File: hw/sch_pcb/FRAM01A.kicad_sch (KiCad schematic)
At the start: 8 parts, among them IC1 CY15B108QN-40SXI, J1 HEADER_2x03_PARALLEL, J2 HEADER_2x04

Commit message: pcb layout update, ready for check
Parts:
- removed C1: 100nF, Mlab_R:SMD-0805, symbol DATALOGGER01A-rescue:C-device
- removed H1, H2, H3, H4: MountingHole_Pad, Mlab_Mechanical:MountingHole_3mm, symbol Mechanical:MountingHole_Pad
- removed J1: HEADER_2x03_PARALLEL, Mlab_Pin_Headers:Straight_2x03, symbol MLAB_HEADER:HEADER_2x03_PARALLEL
- added C1: 10uF, Capacitor_SMD:C_0805_2012Metric, symbol ISM02A-rescue:C_Small-Device-ISM02A-rescue
- added C2: 100nF, Capacitor_SMD:C_0805_2012Metric, symbol ISM02A-rescue:C_Small-Device-ISM02A-rescue
- added D1: BZV55C-5,6V, Diode_SMD:D_SMA, symbol ISM02A-rescue:D_ZENER-MLAB_D
- added J1: Umin ... Umax, Mlab_Pin_Headers:Straight_2x03, symbol header:HEADER_2x03_PARALLEL
- added M1, M2: HOLE M3, Mlab_Mechanical:MountingHole_3mm, symbol mlab-default-rescue:HOLE
- added M3, M4: HOLE, Mlab_Mechanical:MountingHole_3mm, symbol mlab-default-rescue:HOLE
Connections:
- net GND: now also C1.2, C2.2, D1.2 (A), J1.1, J1.2, J1.5, J1.6, M1.1, M2.1, M3.1, M4.1
- net VDD renamed +3.3V
- net +3.3V: now also C1.1, C2.1, D1.1 (K), J1.3, J1.4
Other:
- note added: "MOUNTING HOLES"
- note added: "POWER INPUT"
- note removed: "Mounting holes"

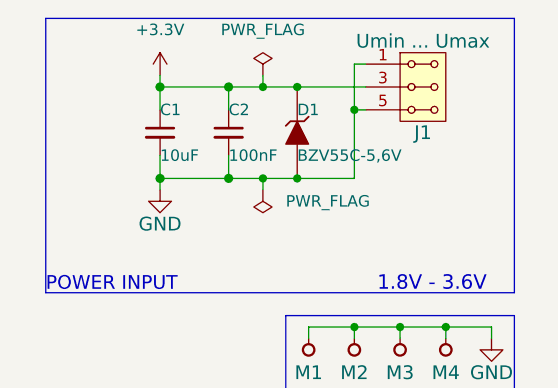
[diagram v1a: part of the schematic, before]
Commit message: smaller pcb layout 1x2
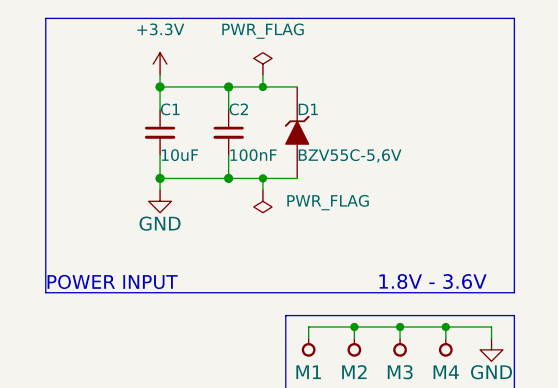
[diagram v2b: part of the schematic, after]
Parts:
- removed J1: Umin ... Umax, Mlab_Pin_Headers:Straight_2x03, symbol header:HEADER_2x03_PARALLEL
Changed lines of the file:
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@@
   (junction (at 241.3 35.56) (diameter 1.016) (color 0 0 0 0)
   )
-  (junction (at 256.54 25.4) (diameter 0) (color 0 0 0 0)
-  )
   (junction (at 252.73 35.56) (diameter 0) (color 0 0 0 0)
   )
-  (junction (at 262.89 27.94) (diameter 0) (color 0 0 0 0)
-  )
   (junction (at 241.3 25.4) (diameter 1.016) (color 0 0 0 0)
   )
   (junction (at 252.73 25.4) (diameter 0) (color 0 0 0 0)
-  )
-  (junction (at 256.54 35.56) (diameter 0) (color 0 0 0 0)
   )
   (no_connect (at 153.67 88.9))
@@
     (stroke (width 0) (type solid) (color 0 0 0 0))
   )
-  (wire (pts (xy 262.89 35.56) (xy 256.54 35.56))
-    (stroke (width 0) (type default) (color 0 0 0 0))
-  )
   (wire (pts (xy 248.92 25.4) (xy 248.92 27.94))
     (stroke (width 0) (type solid) (color 0 0 0 0))
@@
     (stroke (width 0) (type default) (color 0 0 0 0))
   )
-  (wire (pts (xy 264.16 22.86) (xy 262.89 22.86))
-    (stroke (width 0) (type default) (color 0 0 0 0))
-  )
   (wire (pts (xy 125.73 91.44) (xy 128.27 91.44))
     (stroke (width 0) (type default) (color 0 0 0 0))
@@
     (stroke (width 0) (type default) (color 0 0 0 0))
   )
-  (wire (pts (xy 256.54 25.4) (xy 264.16 25.4))
-    (stroke (width 0) (type default) (color 0 0 0 0))
-  )
   (polyline (pts (xy 280.67 60.96) (xy 255.27 60.96))
     (stroke (width 0) (type default) (color 0 0 0 0))
@@
     (stroke (width 0) (type default) (color 0 0 0 0))
   )
-  (wire (pts (xy 262.89 22.86) (xy 262.89 27.94))
-    (stroke (width 0) (type default) (color 0 0 0 0))
-  )
   (wire (pts (xy 209.55 90.17) (xy 212.09 90.17))
     (stroke (width 0) (type default) (color 0 0 0 0))
@@
   )
   (wire (pts (xy 209.55 95.25) (xy 210.82 95.25))
-    (stroke (width 0) (type default) (color 0 0 0 0))
-  )
-  (wire (pts (xy 264.16 27.94) (xy 262.89 27.94))
-    (stroke (width 0) (type default) (color 0 0 0 0))
-  )
-  (wire (pts (xy 262.89 27.94) (xy 262.89 35.56))
     (stroke (width 0) (type default) (color 0 0 0 0))
   )
@@
   (symbol (lib_id "power:+3.3V") (at 241.3 24.13 0) (unit 1)
     (in_bom yes) (on_board yes) (fields_autoplaced)
-    (property "Reference" "#PWR?" (id 0) (at 241.3 27.94 0)
+    (property "Reference" "#PWR0102" (id 0) (at 241.3 27.94 0)
       (effects (font (size 1.27 1.27)) hide)
     )
@@
     (pin "1")
   )
-  (symbol (lib_id "header:HEADER_2x03_PARALLEL") (at 270.51 25.4 0) (unit 1)
-    (in_bom yes) (on_board yes)
-    (property "Reference" "J1" (id 0) (at 270.51 30.48 0)
-      (effects (font (size 1.524 1.524)))
-    )
-    (property "Value" "Umin ... Umax" (id 1) (at 270.51 20.32 0)
-      (effects (font (size 1.524 1.524)))
-    )
-    (property "Footprint" "Mlab_Pin_Headers:Straight_2x03" (id 2) (at 270.51 22.86 0)
-      (effects (font (size 1.524 1.524)) hide)
-    )
-    (property "Datasheet" "" (id 3) (at 270.51 22.86 0)
-      (effects (font (size 1.524 1.524)))
-    )
-    (pin "1")
-    (pin "2")
-    (pin "3")
-    (pin "4")
-    (pin "5")
-    (pin "6")
-  )
   (symbol (lib_id "power:+3.3V") (at 212.09 85.09 0) (unit 1)
     (in_bom yes) (on_board yes) (fields_autoplaced)
@@
     )
     (path "/3b5029ba-e2ce-4aa9-a976-4d3241d2d436"
-      (reference "#PWR?") (unit 1) (value "+3.3V") (footprint "")
+      (reference "#PWR0102") (unit 1) (value "+3.3V") (footprint "")
     )
     (path "/ef59e19a-a355-40db-84c6-ff65a722a099"
@@
       (reference "IC1") (unit 1) (value "CY15B108QN-40SXI") (footprint "KiCad:SOIC127P800X203-8N")
     )
-    (path "/5ef6b1ae-b5ee-4445-9bae-a4ed2e980ea9"
-      (reference "J1") (unit 1) (value "Umin ... Umax") (footprint "Mlab_Pin_Headers:Straight_2x03")
-    )
     (path "/e14eb021-14a8-4312-88f7-4caeccd6d681"

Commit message: Fix DRC and ERC errors. Update title block.
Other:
- title: (none) -> FRAM01A
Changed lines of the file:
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@@
 (kicad_sch (version 20211123) (generator eeschema)
   (paper "A4")
+  (title_block
+    (title "FRAM01A")
+    (date "2023-06-09")
+  )
   (junction (at 210.82 95.25) (diameter 0) (color 0 0 0 0)
   )
